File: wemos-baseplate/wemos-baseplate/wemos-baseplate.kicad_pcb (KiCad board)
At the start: 4 copper layers, 138.4 x 58.4 mm, 18 parts, among them J1 Conn_02x16_Odd_Even, J10 Conn_01x04, J11 Conn_01x04, J12 Conn_01x04, J13 Conn_01x04, J14 Conn_01x04, J15 Conn_01x04, J2 Conn_02x16_Odd_Even, J3 Conn_01x04, J4 Conn_01x04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

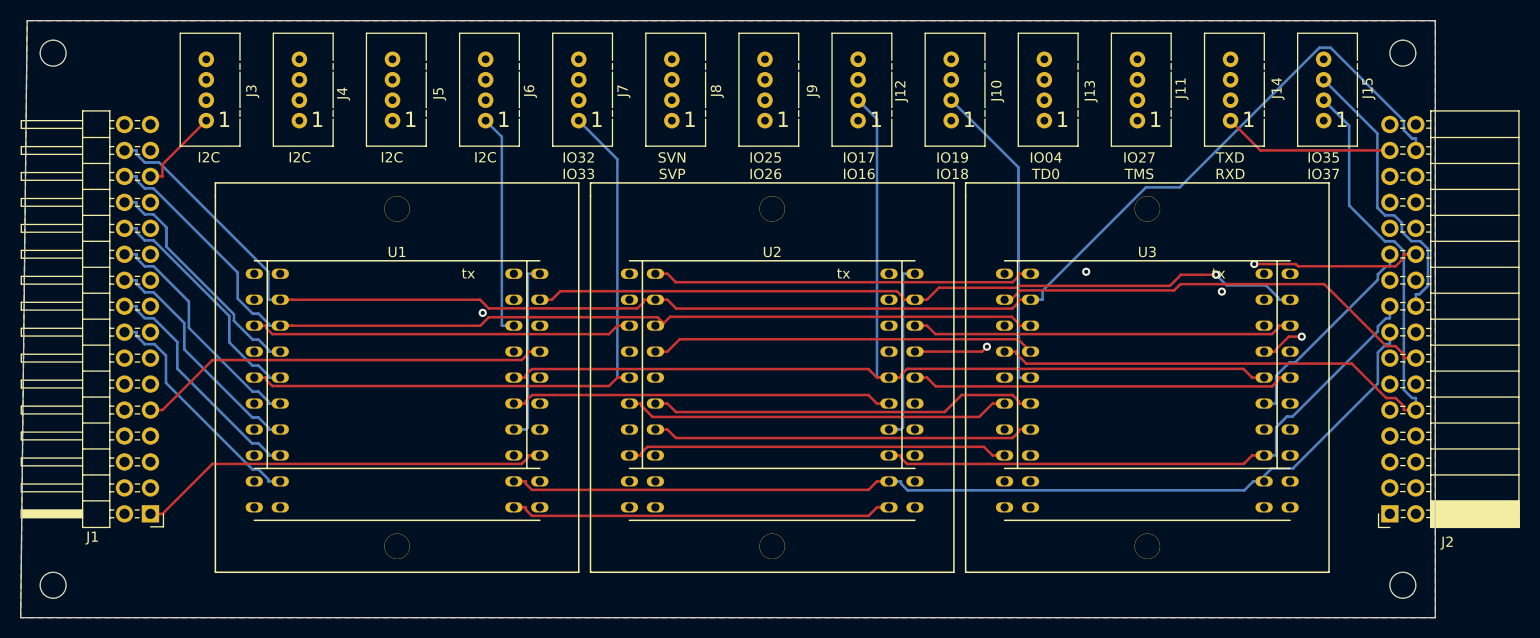
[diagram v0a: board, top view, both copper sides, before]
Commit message: corrected library, still a few nets on the board to fix
in2tech library in separate path
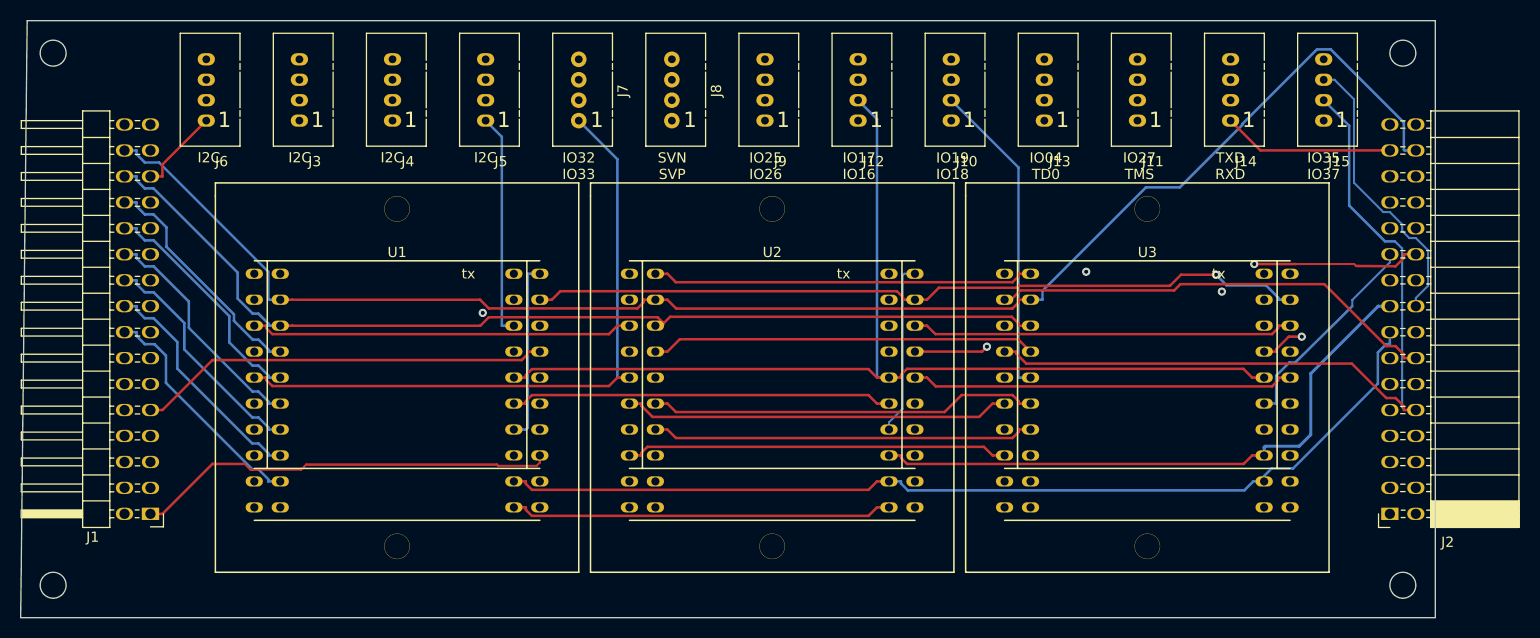
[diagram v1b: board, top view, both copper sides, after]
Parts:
- J1: footprint Connector_PinHeader_2.54mm:PinHeader_2x16_P2.54mm_Horizontal -> in2tech:PinHeader_2x16_P2.54mm_Horizontal_oval
- J10, J11, J12, J13, J14, J15, J9: footprint Connectors:Grove_1x04 -> in2tech:Grove_1x04_oval
- J2: footprint Connector_PinSocket_2.54mm:PinSocket_2x16_P2.54mm_Horizontal -> in2tech:PinSocket_2x16_P2.54mm_Horizontal_oval
- J3: renamed from J4; footprint Connectors:Grove_1x04 -> in2tech:Grove_1x04_oval
- J4: renamed from J5; footprint Connectors:Grove_1x04 -> in2tech:Grove_1x04_oval
- J5: renamed from J6; footprint Connectors:Grove_1x04 -> in2tech:Grove_1x04_oval
- J6: renamed from J3; footprint Connectors:Grove_1x04 -> in2tech:Grove_1x04_oval
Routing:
- net /IO18: track 186.3 -> 201.9 mm
- net /GND: track 295.0 -> 296.9 mm
- net /TMS: track 169.8 -> 171.5 mm
- net /IO02: track 127.9 -> 129.5 mm
- net /IO25: track 169.4 -> 170.9 mm
- net /5V: track 163.9 -> 165.4 mm
- net /RST: track 141.7 -> 142.8 mm
- net /TDI: track 127.9 -> 129.0 mm
- net /3.3V: track 261.9 -> 262.9 mm
- net /IO00: track 127.9 -> 128.8 mm
- net /IO19: track 201.9 -> 202.8 mm
- net /NC2: track 134.9 -> 135.4 mm
- removed copper zone on F.Cu, net /3.3V
- removed copper zone on B.Cu, net /GND
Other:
- rule trace_min: 0.2 -> 0

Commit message: final version before graphics
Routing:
- net /IO27: track 149.4 -> 181.6 mm, vias 2 -> 0
- net /SDA: track 170.5 -> 191.0 mm, vias 1 -> 0
- net /IO23: track 143.4 -> 158.3 mm, vias 1 -> 0
- net /SVN: track 157.8 -> 164.2 mm
- net /IO35: track 168.7 -> 174.6 mm
- net /3.3V: track 262.9 -> 267.8 mm
- net /TCK: track 150.2 -> 153.8 mm
- net /IO19: track 202.8 -> 205.3 mm
- net /GND: track 296.9 -> 298.9 mm
- net /IO26: track 169.5 -> 168.0 mm, vias 1 -> 0
- net /5V: track 165.4 -> 166.8 mm
- net /NC2: track 135.4 -> 136.6 mm
- net /RXD: track 151.0 -> 152.1 mm, vias 1 -> 0
- net /TXD: track 152.5 -> 153.1 mm
- net /SVP: track 171.2 -> 171.8 mm
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- added copper zone on B.Cu, net /GND
- added copper zone on F.Cu, net /GND
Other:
- board size 138.4 x 58.4 mm -> 138 x 55 mm

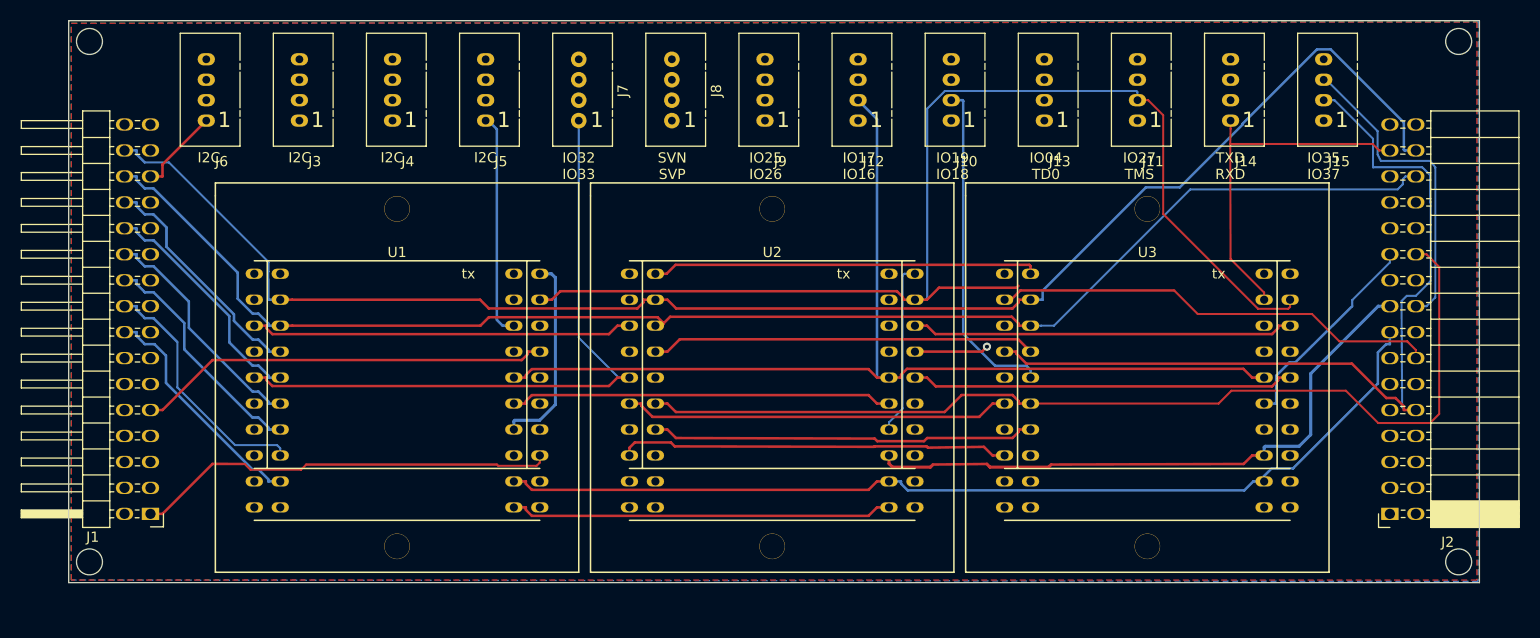
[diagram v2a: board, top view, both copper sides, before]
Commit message: added mount holes for ttgo board
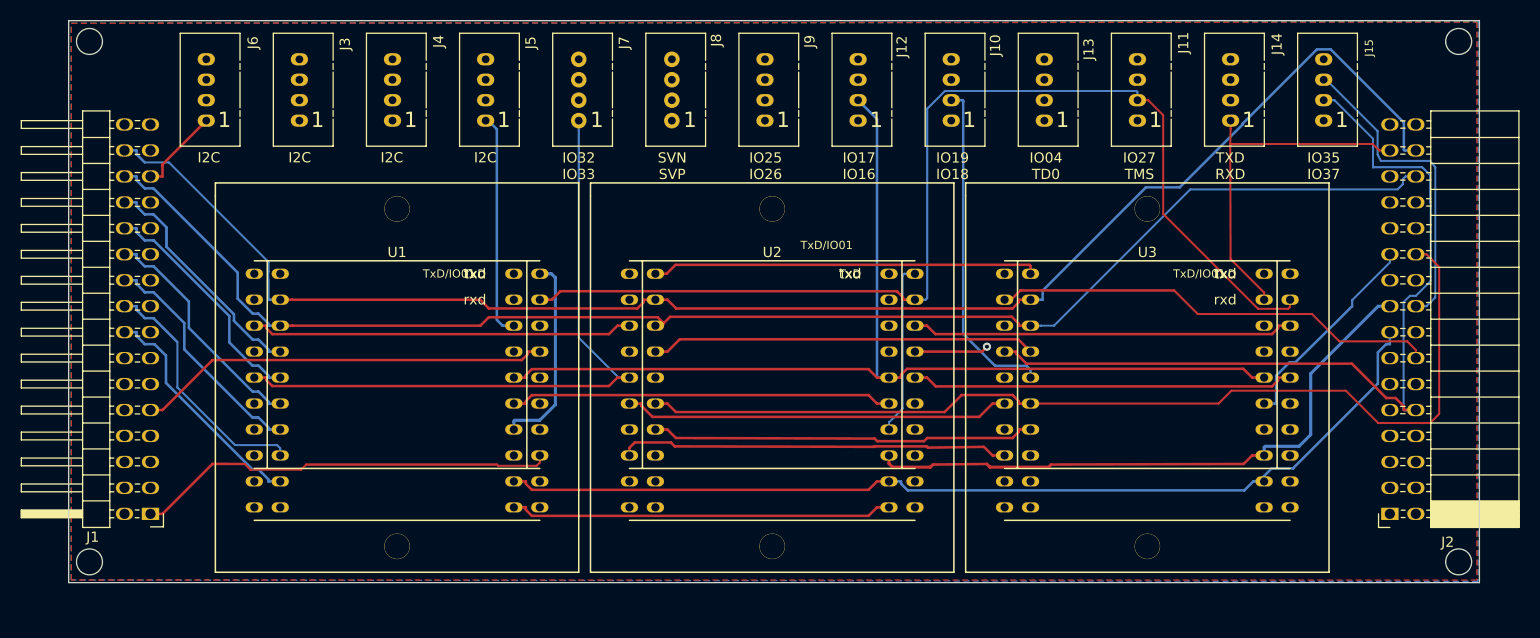
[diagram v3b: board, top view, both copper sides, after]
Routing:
- net /IO27: track 181.6 -> 170.9 mm
- net /GND: track 298.9 -> 290.1 mm
- net /IO35: track 174.6 -> 175.5 mm
